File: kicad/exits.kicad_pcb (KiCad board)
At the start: 2 copper layers, 39.3 x 106.5 mm, 54 parts, among them J1 PJ301M12, J12 Euro power header, J13 PJ301M12, J14 PJ301M12, J2 PJ301M12, J3 PJ301M12, J4 PJ301M12, J5 Attenuator Jumper 1, J6 Attenuator Jumper 2, U1 TL074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

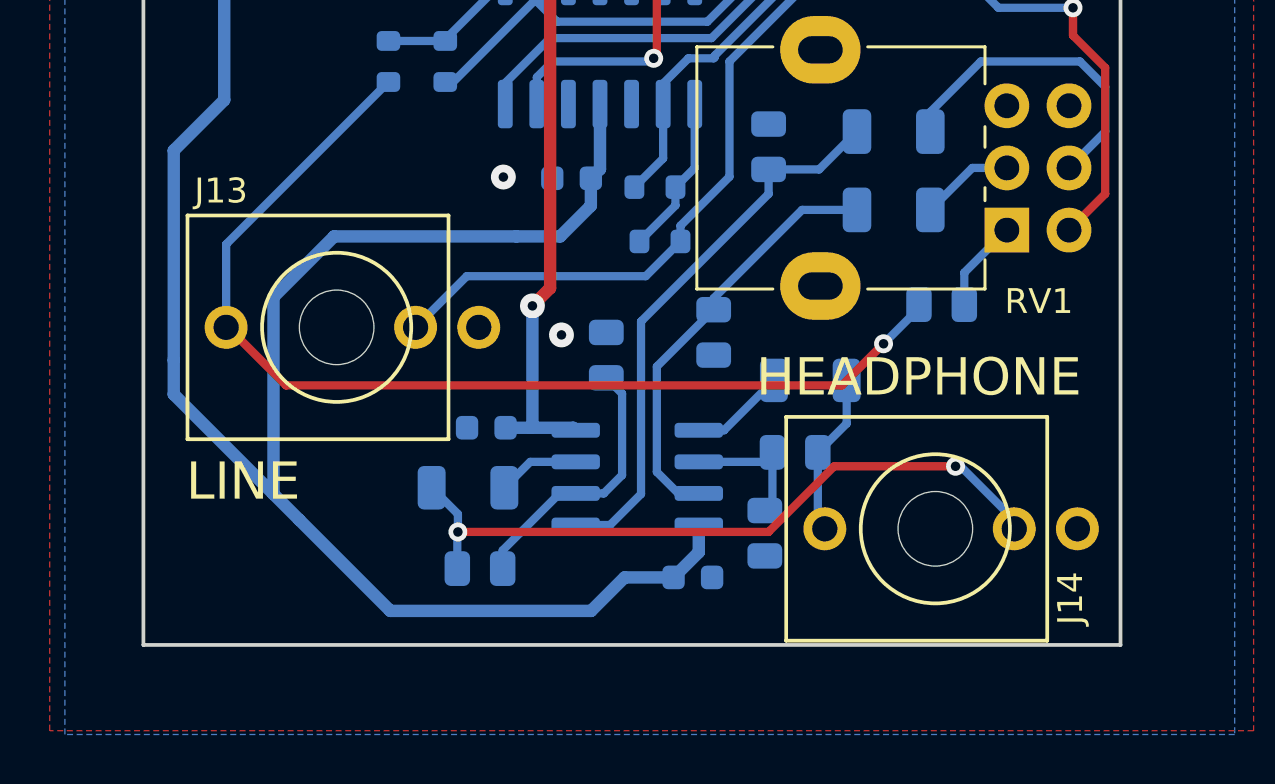
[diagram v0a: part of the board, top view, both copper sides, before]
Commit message: switch to PJ358s for stereo output
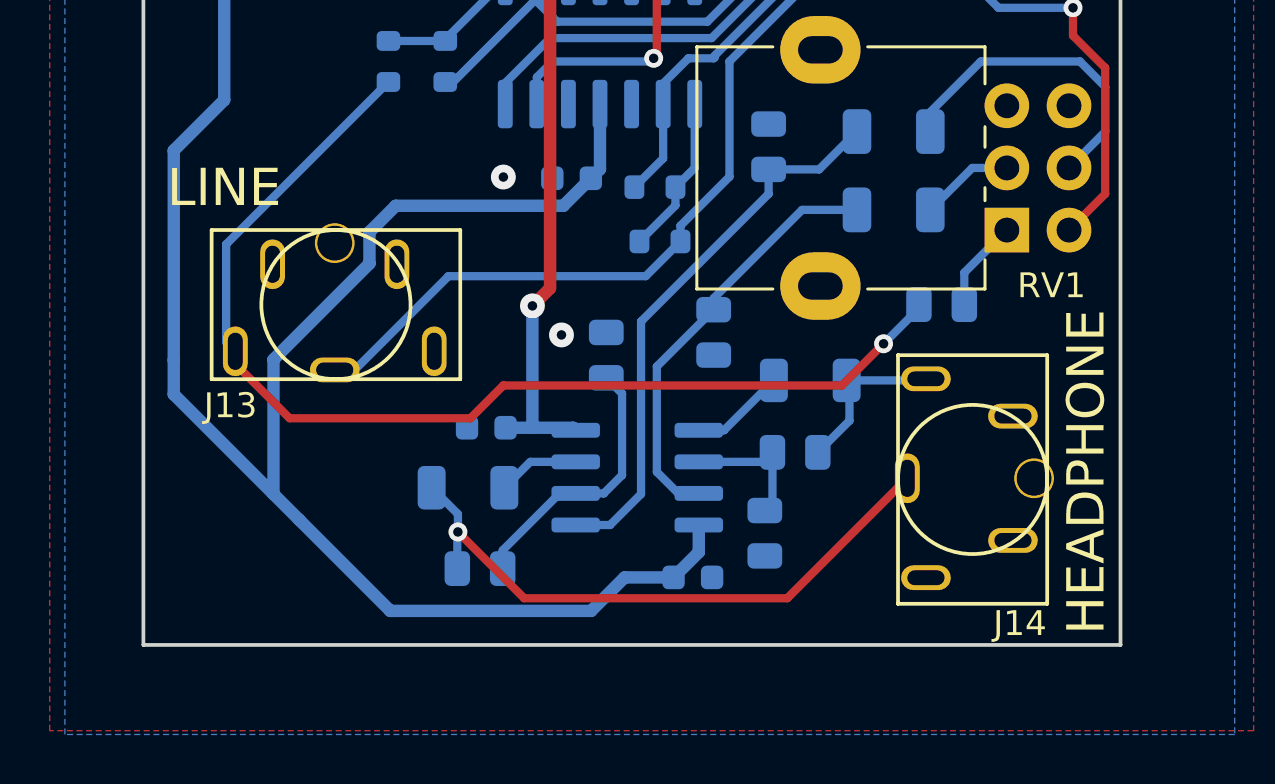
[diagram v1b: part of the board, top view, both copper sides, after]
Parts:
- J13: value PJ301M12 -> PJ358; footprint nearness:PJ301M12 -> nearness:PJ358
- J14: footprint nearness:PJ301M12 -> nearness:PJ358
- moved J14 2.45 mm to (47.5, 125.3)
- moved J13 0.79 mm to (22.0, 118.5), turned to 180 degrees
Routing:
- net RLineOut: track 29.4 -> 33.3 mm
- net HPoutR: track 28.4 -> 24.9 mm, vias 2 -> 1
- net LLineOut: track 42.8 -> 44.6 mm
- net -12V: track 75.4 -> 74.1 mm

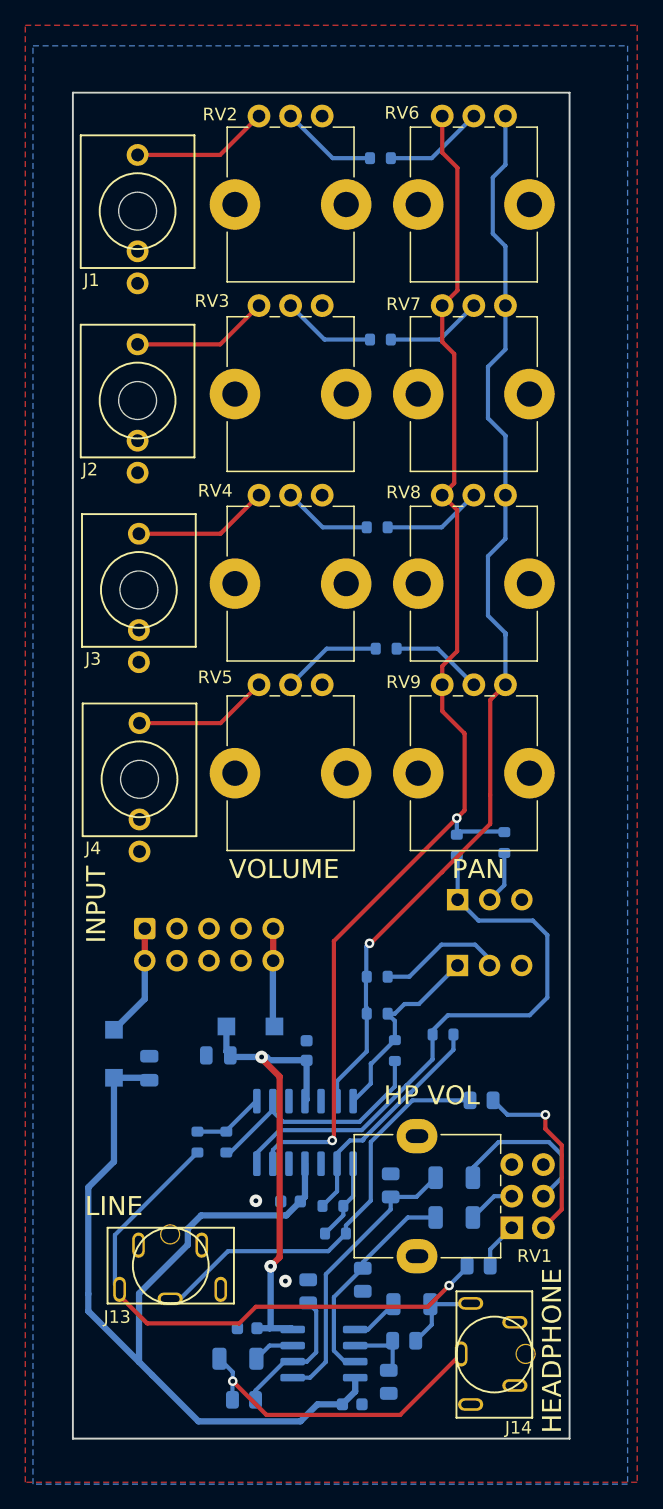
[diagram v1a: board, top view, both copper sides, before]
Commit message: switch to PJ341s, add linearizing Rs
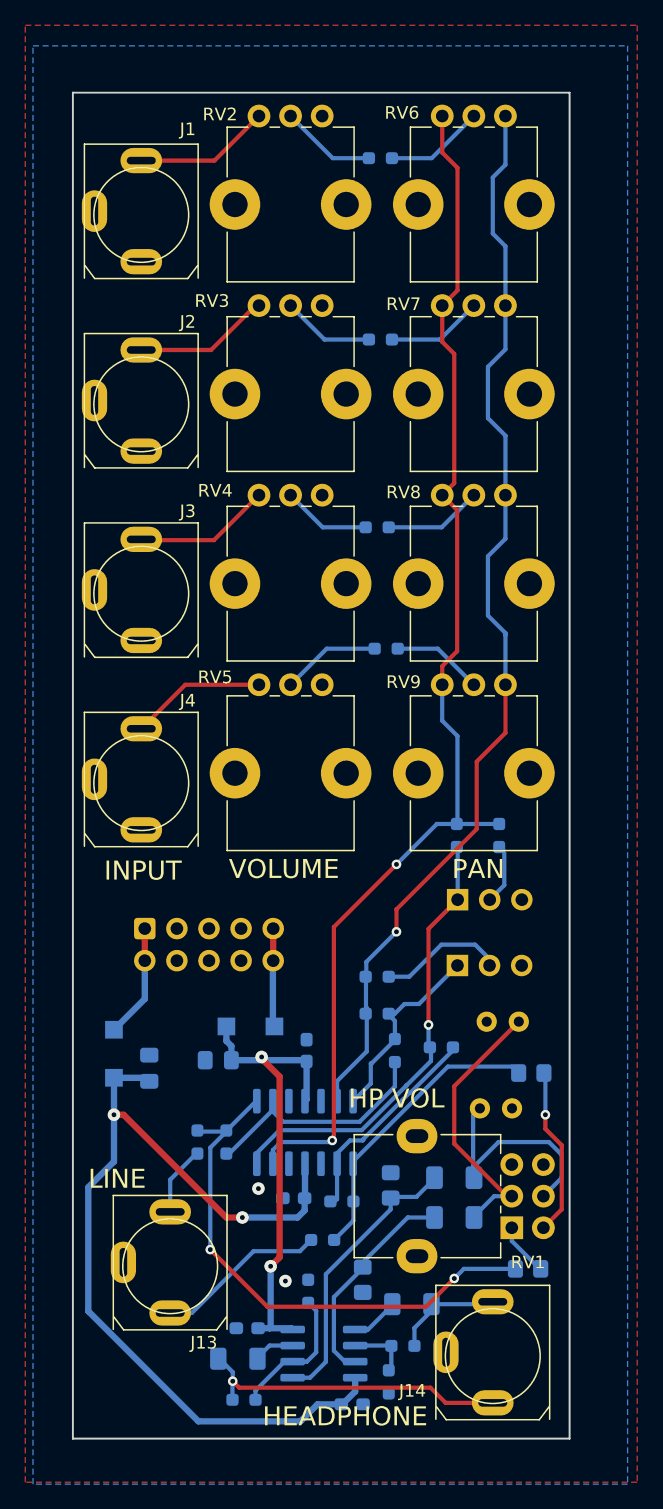
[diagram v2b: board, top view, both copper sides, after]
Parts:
- added R2: LIN1.5K, Resistor_THT:R_Axial_DIN0207_L6.3mm_D2.5mm_P2.54mm_Vertical, B.Cu at (46.5, 105.9)
- added R4: LIN1.5K, Resistor_THT:R_Axial_DIN0207_L6.3mm_D2.5mm_P2.54mm_Vertical, B.Cu at (49.6, 99.1)
- C1, C2: footprint Capacitor_SMD:C_1206_3216Metric -> Capacitor_SMD:C_1206_3216Metric_Pad1.33x1.80mm_HandSolder
- C10, C7, C8, C9: footprint Capacitor_SMD:C_0603_1608Metric -> Capacitor_SMD:C_0603_1608Metric_Pad1.08x0.95mm_HandSolder
- C5, C6: footprint Capacitor_SMD:C_0805_2012Metric -> Capacitor_SMD:C_0805_2012Metric_Pad1.18x1.45mm_HandSolder
- J1, J2, J3, J4: value PJ301M12 -> PJ341; footprint nearness:PJ301M12 -> nearness:PJ341
- J13: value PJ358 -> PJ341; footprint nearness:PJ358 -> nearness:PJ341
- J14: value PJ301M12 -> PJ341; footprint nearness:PJ358 -> nearness:PJ341
- R1, R17, R19, R20, R21, R22, R27, R28, R29, R3, R30, R38, R5, R7: footprint Resistor_SMD:R_0603_1608Metric -> Resistor_SMD:R_0603_1608Metric_Pad0.98x0.95mm_HandSolder
- R15, R16, R35, R36: footprint Resistor_SMD:R_0805_2012Metric -> Resistor_SMD:R_0805_2012Metric_Pad1.20x1.40mm_HandSolder
- R23, R24, R25, R26: footprint Resistor_SMD:R_0805_2012Metric -> Resistor_SMD:R_0603_1608Metric_Pad0.98x0.95mm_HandSolder
- R33, R34: footprint Resistor_SMD:R_1206_3216Metric -> Resistor_SMD:R_1206_3216Metric_Pad1.30x1.75mm_HandSolder
- moved R36 4.49 mm to (50.5, 103.1)
- moved R35 3.92 mm to (50.3, 118.6)
- moved R30 1.14 mm to (34.0, 116.3), turned to 180 degrees
- moved R22 1.02 mm to (43.4, 101.1)
- moved R28 0.80 mm to (35.6, 113.3)
- moved R20 0.76 mm to (44.7, 84.3)
- moved R19 0.69 mm to (48.0, 84.3)
- moved R25 0.42 mm to (40.4, 124.7)
- moved C5 0.38 mm to (25.8, 102.1)
- moved J13 0.38 mm to (22.0, 118.1)
- moved C8 0.36 mm to (31.8, 113.0)
- moved J1 0.29 mm to (19.7, 34.9), turned to 180 degrees
- moved J2 0.29 mm to (19.7, 49.9), turned to 180 degrees
- moved J3 0.19 mm to (19.7, 64.9), turned to 180 degrees
- moved J4 0.14 mm to (19.7, 79.9), turned to 180 degrees
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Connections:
- R27 pad 2: Net-(R27-Pad2) -> Lout
- R28 pad 2: Net-(R28-Pad2) -> Rout
- R29 pad 1: Net-(R27-Pad2) -> Lout
- R30 pad 1: Net-(R28-Pad2) -> Rout
- R35 pad 2: LLineOut -> Lout
- R36 pad 2: RLineOut -> Rout
- RV3 pad 1: Net-(RV3-Pad1) -> Net-(J2-PadT)
- RV4 pad 1: Net-(RV4-Pad1) -> Net-(J3-PadT)
- U1 pad 1: Net-(R27-Pad2) -> Lout
- U1 pad 8: Net-(R28-Pad2) -> Rout
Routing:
- net Lout: track 0.00 -> 43.0 mm, vias 0 -> 2
- net LLineOut: track 44.6 -> 5.59 mm, vias 1 -> 0
- net Rout: track 0.00 -> 23.3 mm
- net RLineOut: track 33.3 -> 13.5 mm
- net Net-(C1-Pad1): track 3.78 -> 21.8 mm
- net Net-(J6-Pad1): track 47.0 -> 35.6 mm, vias 0 -> 1
- net Net-(RV3-Pad1): track 10.9 -> 0.00 mm
- net Net-(J3-PadT): track 0.00 -> 10.8 mm
- net Net-(J2-PadT): track 0.00 -> 10.8 mm
- net Net-(RV4-Pad1): track 10.8 -> 0.00 mm
- net Net-(R28-Pad2): track 6.45 -> 0.00 mm
- net Net-(R27-Pad2): track 5.77 -> 0.00 mm
- net Net-(C2-Pad1): track 13.0 -> 18.7 mm
- net -12V: track 74.1 -> 71.4 mm, vias 0 -> 2
- net HPoutL: track 6.68 -> 8.93 mm
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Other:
- board text added: "HEAR by Crows Electromusic"
- board text removed: "MOUTH by Crows Electromusic"
